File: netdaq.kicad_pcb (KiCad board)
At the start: 2 copper layers, 1 part, among them U1 PIC32CK1025GC01100-I/4SB

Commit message: did alot of stuff
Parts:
- added C1: 100n, Capacitor_SMD:C_0402_1005Metric, F.Cu at (186.1, 102.2)
- added C10: 100n, Capacitor_SMD:C_0402_1005Metric, F.Cu at (189.0, 108.1)
- added C11: 100n, Capacitor_SMD:C_0402_1005Metric, F.Cu at (189.0, 110.0)
- added C12: 100n, Capacitor_SMD:C_0402_1005Metric, F.Cu at (191.9, 102.2)
- added C13: 47u, Capacitor_SMD:C_1210_3225Metric, F.Cu at (181.9, 107.5)
- added C14: 100n, Capacitor_SMD:C_0402_1005Metric, F.Cu at (191.9, 104.1)
- added C15: 4.7u, Capacitor_SMD:C_0805_2012Metric, F.Cu at (186.9, 112.5)
- added C16: 100n, Capacitor_SMD:C_0402_1005Metric, F.Cu at (191.9, 106.1)
- added C17: 10u, Capacitor_SMD:C_0805_2012Metric, F.Cu at (186.9, 115.5)
- added C18: 47u, Capacitor_SMD:C_1210_3225Metric, F.Cu at (181.9, 111.8)
- added C19: C, Capacitor_SMD:C_0402_1005Metric, F.Cu at (180.2, 77.5)
- added C2: 100n, Capacitor_SMD:C_0402_1005Metric, F.Cu at (186.1, 104.1)
- added C20: C, Capacitor_SMD:C_0402_1005Metric, F.Cu at (180.2, 79.5)
- added C21: C, Capacitor_SMD:C_0402_1005Metric, F.Cu at (180.2, 81.4)
- added C22: C, Capacitor_SMD:C_0402_1005Metric, F.Cu at (180.2, 83.4)
- added C23: 1u, Capacitor_SMD:C_0603_1608Metric, F.Cu at (159.4, 72.5)
- added C24: C, Capacitor_SMD:C_0402_1005Metric, F.Cu at (172.4, 71.4)
- added C25: C, Capacitor_SMD:C_0402_1005Metric, F.Cu at (172.4, 73.4)
- added C26: 100n, Capacitor_SMD:C_0402_1005Metric, F.Cu at (172.4, 75.3)
- added C27: 100n, Capacitor_SMD:C_0402_1005Metric, F.Cu at (172.4, 77.3)
- added C28: 1u, Capacitor_SMD:C_0603_1608Metric, F.Cu at (159.4, 76.8)
- added C29: 1u, Capacitor_SMD:C_0603_1608Metric, F.Cu at (159.4, 81.0)
- added C3: 100n, Capacitor_SMD:C_0402_1005Metric, F.Cu at (186.1, 106.1)
- added C30: 100n, Capacitor_SMD:C_0402_1005Metric, F.Cu at (172.4, 79.3)
- added C31: 1u, Capacitor_SMD:C_0603_1608Metric, F.Cu at (159.4, 85.3)
- added C32: 470p, Capacitor_SMD:C_0402_1005Metric, F.Cu at (172.4, 81.3)
- added C4: 100n, Capacitor_SMD:C_0402_1005Metric, F.Cu at (186.1, 108.1)
- added C5: 100n, Capacitor_SMD:C_0402_1005Metric, F.Cu at (186.1, 110.0)
- added C6: 100n, Capacitor_SMD:C_0402_1005Metric, F.Cu at (189.0, 102.2)
- added C7: 100n, Capacitor_SMD:C_0402_1005Metric, F.Cu at (189.0, 104.1)
- added C8: 100n, Capacitor_SMD:C_0402_1005Metric, F.Cu at (189.0, 106.1)
- added C9: 47u, Capacitor_SMD:C_1210_3225Metric, F.Cu at (181.9, 103.3)
- added D1: LED, LED_SMD:LED_0805_2012Metric, F.Cu at (181.0, 71.9)
- added D2: LED, LED_SMD:LED_0805_2012Metric, F.Cu at (181.0, 75.0)
- added D3: LED, LED_SMD:LED_0805_2012Metric, F.Cu at (170.8, 85.9)
- added D4: LED, LED_SMD:LED_0805_2012Metric, F.Cu at (170.8, 88.9)
- added R1: 0, Resistor_SMD:R_0402_1005Metric, F.Cu at (190.6, 112.0)
- added R10: 1.5k, Resistor_SMD:R_0402_1005Metric, F.Cu at (163.7, 71.4)
- added R11: 1.5k, Resistor_SMD:R_0402_1005Metric, F.Cu at (163.7, 73.4)
- added R12: 33, Resistor_SMD:R_0402_1005Metric, F.Cu at (163.7, 75.4)
- added R13: 33, Resistor_SMD:R_0402_1005Metric, F.Cu at (163.7, 77.4)
- added R14: 33, Resistor_SMD:R_0402_1005Metric, F.Cu at (163.7, 79.4)
- added R15: 10k, Resistor_SMD:R_0402_1005Metric, F.Cu at (163.7, 81.4)
- added R16: 10k, Resistor_SMD:R_0402_1005Metric, F.Cu at (163.7, 83.4)
- added R17: 10k, Resistor_SMD:R_0402_1005Metric, F.Cu at (166.6, 71.4)
- added R18: 10k, Resistor_SMD:R_0402_1005Metric, F.Cu at (166.6, 73.4)
- added R19: 10k, Resistor_SMD:R_0402_1005Metric, F.Cu at (166.6, 75.4)
- added R2: 0, Resistor_SMD:R_0402_1005Metric, F.Cu at (190.6, 114.0)
- added R20: 10k, Resistor_SMD:R_0402_1005Metric, F.Cu at (166.6, 77.4)
- added R21: 1.5k, Resistor_SMD:R_0402_1005Metric, F.Cu at (166.6, 79.4)
- added R22: 10k, Resistor_SMD:R_0402_1005Metric, F.Cu at (166.6, 81.4)
- added R23: 10k, Resistor_SMD:R_0402_1005Metric, F.Cu at (166.6, 83.4)
- added R24: 12.1k, Resistor_SMD:R_0402_1005Metric, F.Cu at (169.6, 71.4)
- added R25: R, Resistor_SMD:R_0402_1005Metric, F.Cu at (169.6, 73.4)
- added R26: R, Resistor_SMD:R_0402_1005Metric, F.Cu at (169.6, 75.4)
- added R27: 10k, Resistor_SMD:R_0402_1005Metric, F.Cu at (169.6, 77.4)
- added R28: 10k, Resistor_SMD:R_0402_1005Metric, F.Cu at (169.6, 79.4)
- added R3: R, Resistor_SMD:R_0402_1005Metric, F.Cu at (177.3, 71.4)
- added R4: R, Resistor_SMD:R_0402_1005Metric, F.Cu at (177.3, 73.4)
- added R5: 10k, Resistor_SMD:R_0402_1005Metric, F.Cu at (177.3, 75.4)
- added R6: 10k, Resistor_SMD:R_0402_1005Metric, F.Cu at (177.3, 77.4)
- added R7: 270, Resistor_SMD:R_0402_1005Metric, F.Cu at (177.3, 79.4)
- added R8: 10k, Resistor_SMD:R_0402_1005Metric, F.Cu at (177.3, 81.4)
- added R9: 10k, Resistor_SMD:R_0402_1005Metric, F.Cu at (177.3, 83.4)
- added TR1: PT61017PEL, Transformer_SMD:Transformer_Ethernet_Bourns_PT61017PEL, F.Cu at (149.5, 79.5)
- added U2: LAN8720A-CP, LAN8720A-CP:QFN24-6X6_MC_MCH, F.Cu at (150.4, 91.5)
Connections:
- U1 pad 1: unconnected-(U1A-PA00-Pad1) -> /MCU/JTAG.TDI
- U1 pad 10: unconnected-(U1A-PA15-Pad10) -> /MCU/SPI5.SCK
- U1 pad 100: unconnected-(U1A-PD11-Pad100) -> /MCU/SDMMC0_SDDAT1
- U1 pad 11: unconnected-(U1A-PA16-Pad11) -> /MCU/SPI5.CS#
- U1 pad 12: unconnected-(U1A-PA17-Pad12) -> /MCU/SPARE1
- U1 pad 13: unconnected-(U1A-PA04-Pad13) -> /MCU/SPI7.MISO
- U1 pad 14: unconnected-(U1A-PA05-Pad14) -> /MCU/SPI7.SCK
- U1 pad 15: unconnected-(U1A-PA06-Pad15) -> /MCU/SPI7.CS#
- U1 pad 16: unconnected-(U1A-PA07-Pad16) -> /MCU/SPI6.MOSI
- U1 pad 17: unconnected-(U1A-PA08-Pad17) -> /MCU/SPI6.MISO
- U1 pad 18: unconnected-(U1A-PA18-Pad18) -> /MCU/SPARE2
- U1 pad 2: unconnected-(U1A-PA01-Pad2) -> /MCU/PA01
- U1 pad 20: unconnected-(U1B-VDDIO-Pad20) -> +3.3V
- U1 pad 21: unconnected-(U1A-EXT-Pad21) -> /MCU/EXT
- U1 pad 22: unconnected-(U1A-PA09-Pad22) -> /MCU/SPI6.SCK
- U1 pad 23: unconnected-(U1A-PA10-Pad23) -> /MCU/SPI6.CS#
- U1 pad 24: unconnected-(U1A-PA11-Pad24) -> /SMI.MDC
- U1 pad 25: unconnected-(U1A-PA12-Pad25) -> /SMI.MDIO
- U1 pad 26: unconnected-(U1A-PB00-Pad26) -> /MCU/SPARE12
- U1 pad 27: unconnected-(U1A-PB01-Pad27) -> /MCU/SPARE13
- U1 pad 28: unconnected-(U1A-PB11-Pad28) -> /MCU/ADC_VINP10
- U1 pad 29: unconnected-(U1A-PB12-Pad29) -> /MCU/ADC_VINP11
- U1 pad 3: unconnected-(U1A-PA02-Pad3) -> /MCU/JTAG.TMS
- U1 pad 31: unconnected-(U1A-PB02-Pad31) -> /MCU/XIN32
- U1 pad 32: unconnected-(U1A-PB03-Pad32) -> /MCU/XOUT32
- U1 pad 33: unconnected-(U1B-VDDA-Pad33) -> Net-(U1B-VDDA)
- U1 pad 34: unconnected-(U1B-VDDIO-Pad34) -> +3.3V
- U1 pad 36: unconnected-(U1A-PB04-Pad36) -> /MCU/SPI4.MOSI
- U1 pad 37: unconnected-(U1A-PB05-Pad37) -> /MCU/SPI4.MISO
- U1 pad 38: unconnected-(U1A-PB13-Pad38) -> /MCU/SPI4.SCK
- U1 pad 39: unconnected-(U1A-PB06-Pad39) -> /MCU/SPI4.CS#
- U1 pad 4: unconnected-(U1A-PA03-Pad4) -> /MCU/JTAG.TCK
- U1 pad 40: unconnected-(U1A-PB14-Pad40) -> /MCU/SPARE16
- U1 pad 41: unconnected-(U1A-PB15-Pad41) -> /MCU/SPARE17
- U1 pad 42: unconnected-(U1B-VDDIO-Pad42) -> +3.3V
- U1 pad 44: unconnected-(U1B-VDDREG-Pad44) -> +3.3V
- U1 pad 45: unconnected-(U1A-PB16-Pad45) -> /MCU/SPI3.MOSI
- U1 pad 46: unconnected-(U1A-PB17-Pad46) -> /MCU/SPI3.MISO
- U1 pad 47: unconnected-(U1A-PB07-Pad47) -> /MCU/SPI3.SCK
- U1 pad 48: unconnected-(U1A-PB08-Pad48) -> /MCU/SPI3.CS#
- U1 pad 49: unconnected-(U1A-PB09-Pad49) -> /MCU/SPARE14
- U1 pad 5: unconnected-(U1A-RESET_N-Pad5) -> /MCU/RESET#
- U1 pad 50: unconnected-(U1A-PB10-Pad50) -> /MCU/SPARE15
- U1 pad 51: unconnected-(U1A-PC00-Pad51) -> /MCU/RMII.REFCK
- U1 pad 52: unconnected-(U1A-PC01-Pad52) -> /MCU/SPARE4
- U1 pad 53: unconnected-(U1A-PC02-Pad53) -> /MCU/SPARE5
- U1 pad 54: unconnected-(U1A-PC03-Pad54) -> /MCU/SPARE6
- U1 pad 55: unconnected-(U1A-PC04-Pad55) -> /MCU/SPARE7
- U1 pad 56: unconnected-(U1B-VDDIO-Pad56) -> +3.3V
- U1 pad 58: unconnected-(U1A-PC14-Pad58) -> /MCU/SPARE9
- U1 pad 59: unconnected-(U1A-PC05-Pad59) -> /MCU/SPARE8
- U1 pad 60: unconnected-(U1A-PC06-Pad60) -> /MCU/RMII.RXD1
- U1 pad 61: unconnected-(U1A-PC07-Pad61) -> /MCU/RMII.RXD0
- U1 pad 62: unconnected-(U1B-VDDREG-Pad62) -> +3.3V
- U1 pad 63: unconnected-(U1A-PC09-Pad63) -> /MCU/RMII.RXER
- U1 pad 64: unconnected-(U1A-PC15-Pad64) -> /MCU/SPI2.MOSI
- U1 pad 65: unconnected-(U1A-PC16-Pad65) -> /MCU/SPI2.MISO
- U1 pad 66: unconnected-(U1A-PC17-Pad66) -> /MCU/SPI2.SCK
- U1 pad 67: unconnected-(U1A-PC18-Pad67) -> /MCU/SPI2.CS#
- U1 pad 68: unconnected-(U1A-PC10-Pad68) -> /MCU/RMII.CRSDV
- U1 pad 69: unconnected-(U1B-VDDIO-Pad69) -> +3.3V
- U1 pad 7: unconnected-(U1B-VDDIO-Pad7) -> +3.3V
- U1 pad 71: unconnected-(U1A-PC11-Pad71) -> /MCU/RMII.TXEN
- U1 pad 72: unconnected-(U1A-PC12-Pad72) -> /MCU/RMII.TXD0
- U1 pad 73: unconnected-(U1A-PC13-Pad73) -> /MCU/RMII.TXD1
- U1 pad 74: unconnected-(U1A-PC19-Pad74) -> /MCU/SPARE10
- U1 pad 75: unconnected-(U1A-PC20-Pad75) -> /MCU/SPARE11
- U1 pad 76: unconnected-(U1A-USB0PN-Pad76) -> /MCU/USB_HS.D-
- U1 pad 77: unconnected-(U1A-USB0PP-Pad77) -> /MCU/USB_HS.D+
- U1 pad 78: unconnected-(U1A-USB0ID-Pad78) -> /MCU/USB0ID
- U1 pad 79: unconnected-(U1B-VCCAP3-Pad79) -> +3.3V
- U1 pad 8: unconnected-(U1A-PA13-Pad8) -> /MCU/SPI5.MOSI
- U1 pad 82: unconnected-(U1A-USRBIAS-Pad82) -> /MCU/USRBIAS
- U1 pad 83: unconnected-(U1B-VDDREG-Pad83) -> +3.3V
- U1 pad 85: unconnected-(U1B-VDDIO-Pad85) -> +3.3V
- U1 pad 86: unconnected-(U1A-PD00-Pad86) -> /MCU/XIN
- U1 pad 87: unconnected-(U1A-PD01-Pad87) -> /MCU/XOUT
- U1 pad 88: unconnected-(U1A-PD02-Pad88) -> /MCU/ETH_TSUCOMP
- U1 pad 89: unconnected-(U1A-USB_DM-Pad89) -> /MCU/USB_FS.D-
- U1 pad 9: unconnected-(U1A-PA14-Pad9) -> /MCU/SPI5.MISO
- U1 pad 90: unconnected-(U1A-USB_DP-Pad90) -> /MCU/USB_FS.D+
- U1 pad 91: unconnected-(U1A-PD12-Pad91) -> /MCU/SDMMC0_SDCD
- U1 pad 92: unconnected-(U1A-PD05-Pad92) -> /MCU/SDMMC0_SDWP
- U1 pad 93: unconnected-(U1A-PD06-Pad93) -> /MCU/SDMMC0_SDCMD
- U1 pad 94: unconnected-(U1A-PD07-Pad94) -> /MCU/SDMMC0_SDDAT0
- U1 pad 96: unconnected-(U1B-VDDIO-Pad96) -> +3.3V
- U1 pad 97: unconnected-(U1A-PD08-Pad97) -> /MCU/SDMMC0_SDDAT2
- U1 pad 98: unconnected-(U1A-PD09-Pad98) -> /MCU/SDMMC0_SDDAT3
- U1 pad 99: unconnected-(U1A-PD10-Pad99) -> /MCU/SDMMC0_SDCK

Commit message: did stuff
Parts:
- added J1: RJ45, Connector_RJ:RJ45_Amphenol_54602-x08_Horizontal, F.Cu at (153.3, 66.1)
- added J2: ~, pxc_1713856_02_01_DMC-1-5-19-G1F-3-5-LR-P26THR:pxc_1713856_02_01_DMC-1-5-19-G1F-3-5-LR-P26THR, F.Cu at (170.0, 140.0)
- added TR2: Wuerth_750343373, Transformer_THT:Transformer_Wuerth_750343373, F.Cu at (170.8, 63.8)
- added U3: MP6004GQ-P, MP6004GQ-P:QFN-14_MP6004_MNP, F.Cu at (169.4, 86.0)
- moved C19 59.3 mm to (238.5, 88.1)
- moved C20 59.3 mm to (238.5, 90.1)
- moved C23 59.3 mm to (217.8, 83.2)
- moved C24 59.3 mm to (230.7, 82.0)
- moved C25 59.3 mm to (230.7, 84.0)
- moved C26 59.3 mm to (230.7, 86.0)
- moved C27 59.3 mm to (230.7, 87.9)
- moved C28 59.3 mm to (217.8, 87.4)
- moved C29 59.3 mm to (217.8, 91.7)
- moved C31 59.3 mm to (217.8, 95.9)
- moved D1 59.3 mm to (239.3, 82.5)
- moved R11 59.3 mm to (222.0, 84.0)
- moved R14 59.3 mm to (222.0, 90.0)
- moved R18 59.3 mm to (224.9, 84.0)
- moved R21 59.3 mm to (224.9, 90.0)
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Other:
- board outline added: 72 x 83 mm

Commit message: did stuff
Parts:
- added U4: PD70100ILD-TR, PD70100ILD-TR:DFN12_4X3_MCH, F.Cu at (143.1, 102.2)
- added U5: ~, CDHD01:CDHD01, F.Cu at (138.8, 94.0)
- added U6: ~, CDHD01:CDHD01, F.Cu at (137.8, 79.5)
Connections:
- net Net-(D5-A) renamed /PoE Regulator/FLY_SW
- net Net-(R38-Pad1) renamed /PoE Regulator/FLY_CT
- net Net-(U3-FB1) renamed /PoE Regulator/FLY_FB
- net Net-(U3-VCC) renamed /PoE Regulator/FLY_VCC

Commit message: stuff
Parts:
- added U7: TPS62A01PDDCR, TPS62A01PDDCR:DDC0006A-MFG, F.Cu at (142.8, 116.0)
- moved C19 77.4 mm to (170.8, 125.4)
- moved C20 77.4 mm to (170.8, 127.4)
- moved C21 77.4 mm to (170.8, 129.4)
- moved C22 77.4 mm to (170.8, 131.3)
- moved C23 77.4 mm to (150.0, 120.5)
- moved C24 77.4 mm to (163.0, 119.4)
- moved C25 77.4 mm to (163.0, 121.3)
- moved C26 77.4 mm to (163.0, 123.3)
- moved C27 77.4 mm to (163.0, 125.3)
- moved C28 77.4 mm to (150.0, 124.8)
- moved C29 77.4 mm to (150.0, 129.0)
- moved C30 77.4 mm to (163.0, 127.2)
- moved C31 77.4 mm to (150.0, 133.2)
- moved C32 77.4 mm to (163.0, 129.2)
- moved D1 77.4 mm to (171.6, 119.9)
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
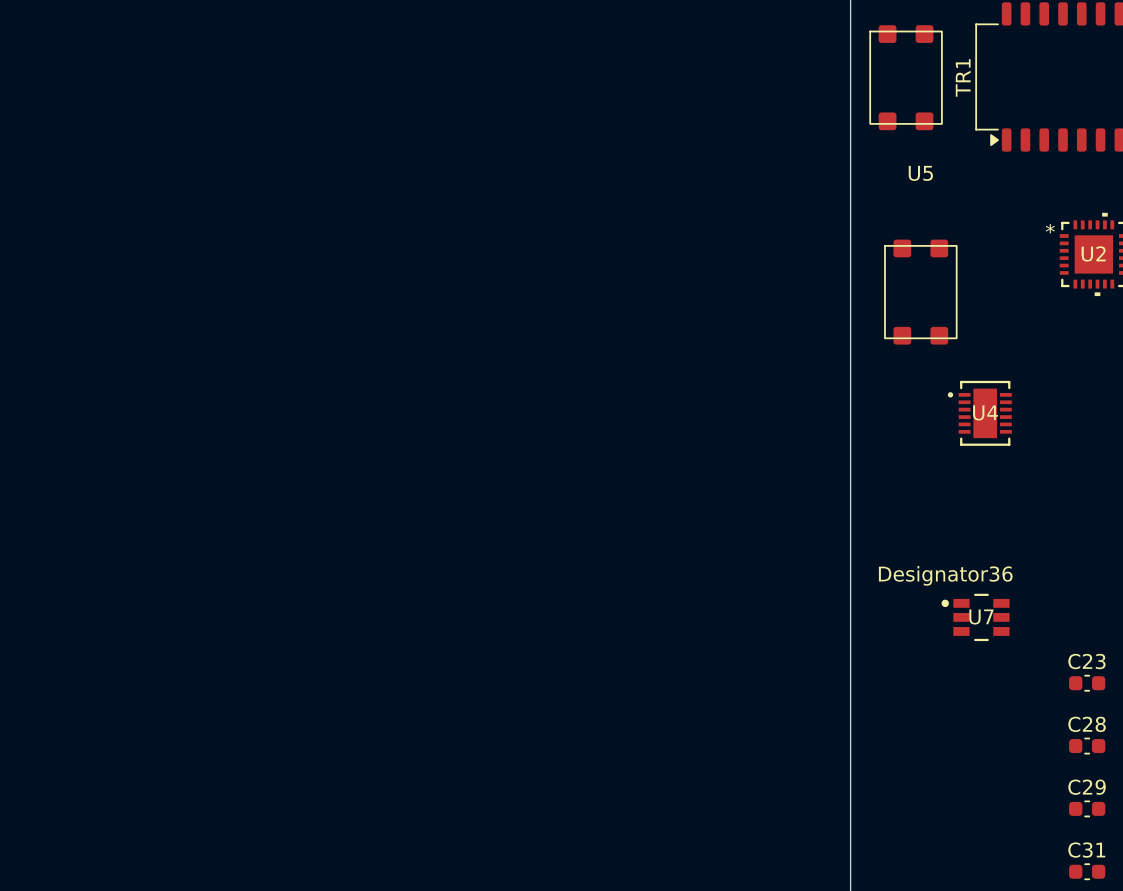
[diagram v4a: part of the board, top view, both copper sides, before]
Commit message: did 3v3 reg
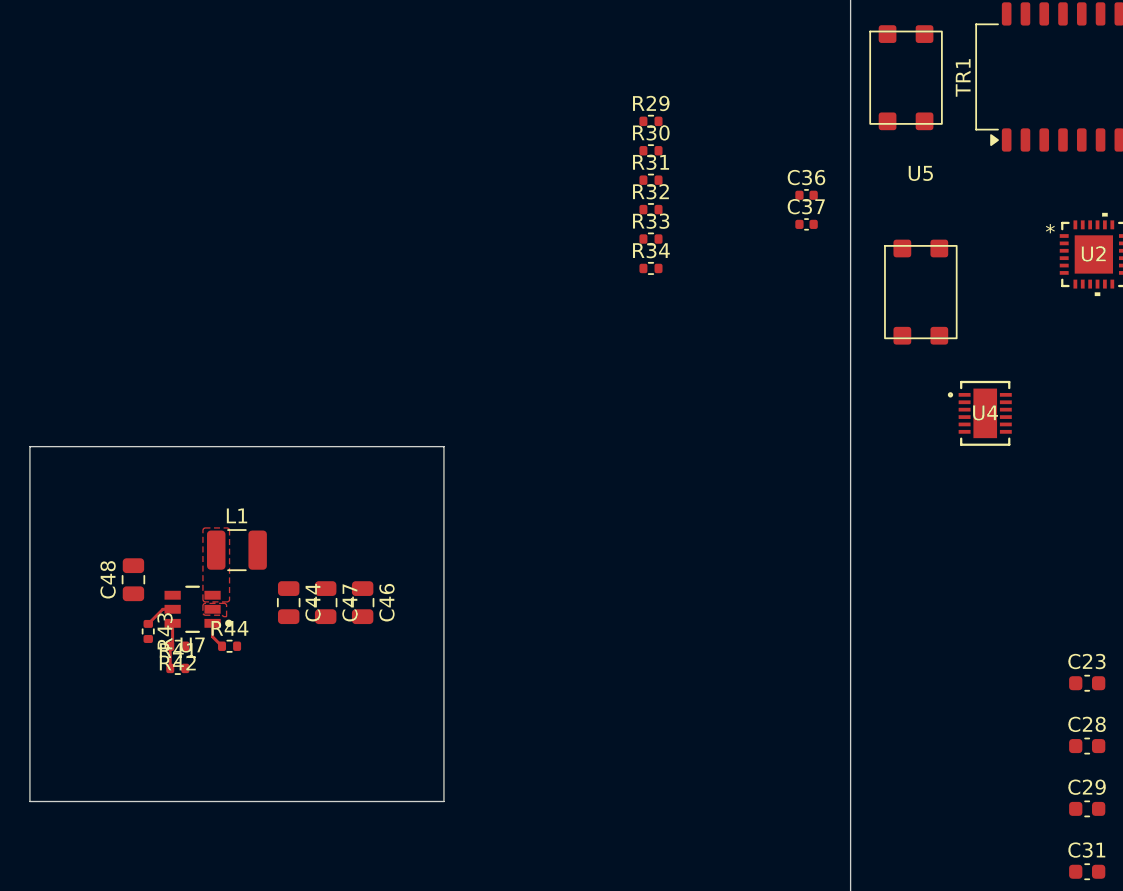
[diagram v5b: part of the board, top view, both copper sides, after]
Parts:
- added C36: 100n, Capacitor_SMD:C_0402_1005Metric, F.Cu at (131.0, 87.5)
- added C37: 100n, Capacitor_SMD:C_0402_1005Metric, F.Cu at (131.0, 89.5)
- added C44: 10u, Capacitor_SMD:C_0805_2012Metric, F.Cu at (96.0, 115.0)
- added C46: 10u, Capacitor_SMD:C_0805_2012Metric, F.Cu at (101.0, 115.0)
- added C47: 10u, Capacitor_SMD:C_0805_2012Metric, F.Cu at (98.5, 115.0)
- added C48: 10u, Capacitor_SMD:C_0805_2012Metric, F.Cu at (85.5, 113.5)
- added L1: 1u, Inductor_SMD:L_1210_3225Metric, F.Cu at (92.5, 111.5)
- added R29: 75, Resistor_SMD:R_0402_1005Metric, F.Cu at (120.5, 82.5)
- added R30: 75, Resistor_SMD:R_0402_1005Metric, F.Cu at (120.5, 84.5)
- added R31: 75, Resistor_SMD:R_0402_1005Metric, F.Cu at (120.5, 86.5)
- added R32: 75, Resistor_SMD:R_0402_1005Metric, F.Cu at (120.5, 88.5)
- added R33: 0, Resistor_SMD:R_0402_1005Metric, F.Cu at (120.5, 90.5)
- added R34: 0, Resistor_SMD:R_0402_1005Metric, F.Cu at (120.5, 92.5)
- added R41: 453k, Resistor_SMD:R_0402_1005Metric, F.Cu at (88.5, 119.5)
- added R42: 100k, Resistor_SMD:R_0402_1005Metric, F.Cu at (88.5, 118.0)
- added R43: 100k, Resistor_SMD:R_0402_1005Metric, F.Cu at (86.5, 117.0)
- added R44: 100k, Resistor_SMD:R_0402_1005Metric, F.Cu at (92.0, 118.0)
- moved U7 53.4 mm to (89.5, 115.5), turned to 180 degrees
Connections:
- U7 pad 1: unconnected-(U7-EN-Pad1) -> /3V3 Regulator/3V3_EN
- U7 pad 2: unconnected-(U7-GND-Pad2) -> GND
- U7 pad 3: unconnected-(U7-SW-Pad3) -> /3V3 Regulator/3V3_SW
- U7 pad 4: unconnected-(U7-VIN-Pad4) -> +5.0V
- U7 pad 5: unconnected-(U7-PG-Pad5) -> /3V3 Regulator/3V3_PG
- U7 pad 6: unconnected-(U7-FB-Pad6) -> /3V3 Regulator/3V3_FB
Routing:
- net /3V3 Regulator/3V3_FB: track 0.00 -> 3.12 mm
- net /3V3 Regulator/3V3_PG: track 0.00 -> 2.06 mm
- net /3V3 Regulator/3V3_EN: track 0.00 -> 1.82 mm
- added copper zone on F.Cu, net /3V3 Regulator/3V3_SW
- added copper zone on F.Cu, net GND
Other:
- board size 72 x 83 mm -> 127.5 x 83 mm
- board text added: "3v3"

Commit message: stuff
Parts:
- added C49: 100n, Capacitor_SMD:C_0402_1005Metric, F.Cu at (231.5, 118.0)
- added C50: 10u, Capacitor_SMD:C_0805_2012Metric, F.Cu at (232.3, 115.5)
- added J3: Conn_01x06_Pin, Connector_PinHeader_2.54mm:PinHeader_1x06_P2.54mm_Vertical, F.Cu at (42.0, 120.3)
- added J4: Micro_SD_Card_Det2, Connector_Card:microSD_HC_Hirose_DM3AT-SF-PEJM5, F.Cu at (221.7, 107.4)
- added R1: 0, Resistor_SMD:R_0402_1005Metric, F.Cu at (129.5, 69.0)
- added R45: 100k, Resistor_SMD:R_0402_1005Metric, F.Cu at (231.5, 99.1)
- added R46: 10k, Resistor_SMD:R_0402_1005Metric, F.Cu at (231.5, 101.1)
- added R47: 10k, Resistor_SMD:R_0402_1005Metric, F.Cu at (231.5, 103.1)
- added R48: 10k, Resistor_SMD:R_0402_1005Metric, F.Cu at (231.5, 105.0)
- added R49: 10k, Resistor_SMD:R_0402_1005Metric, F.Cu at (231.5, 107.0)
- added R50: 10k, Resistor_SMD:R_0402_1005Metric, F.Cu at (231.5, 109.0)
- added R51: 10k, Resistor_SMD:R_0402_1005Metric, F.Cu at (231.5, 111.0)
- added R52: 10k, Resistor_SMD:R_0402_1005Metric, F.Cu at (231.5, 113.0)
- added R53: 0, Resistor_SMD:R_0402_1005Metric, F.Cu at (129.5, 71.0)
- added R54: 0, Resistor_SMD:R_0402_1005Metric, F.Cu at (129.5, 73.0)
- added R55: 0, Resistor_SMD:R_0402_1005Metric, F.Cu at (129.5, 75.0)
- added R56: 27, Resistor_SMD:R_0402_1005Metric, F.Cu at (56.5, 54.0)
- added R57: 27, Resistor_SMD:R_0402_1005Metric, F.Cu at (55.0, 55.5)
- added R58: 27, Resistor_SMD:R_0402_1005Metric, F.Cu at (57.0, 54.5)
- added R59: 27, Resistor_SMD:R_0402_1005Metric, F.Cu at (55.5, 56.0)
- moved C12 125.9 mm to (72.5, 62.1)
- moved C13 125.9 mm to (62.5, 67.4)
- moved C14 125.9 mm to (72.5, 64.0)
- moved C18 125.9 mm to (62.5, 71.7)
- moved C9 125.9 mm to (62.5, 63.2)
- moved C1 125.9 mm to (66.8, 62.1)
- moved C16 125.9 mm to (72.5, 66.0)
- moved C19 125.9 mm to (51.4, 85.3)
- moved C2 125.9 mm to (66.8, 64.0)
- moved C20 125.9 mm to (51.4, 87.3)
- moved C21 125.9 mm to (51.4, 89.3)
- moved C22 125.9 mm to (51.4, 91.3)
- moved C6 125.9 mm to (69.7, 62.1)
- moved C7 125.9 mm to (69.7, 64.0)
- moved D1 125.9 mm to (52.3, 79.8)
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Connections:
- net /MCU/SDMMC0_SDWP renamed /SDMMC.SDWP
- net /MCU/SPI4.CS# renamed /MCU/NC_SERCOM4_PAD3
- net /MCU/SPI4.MISO renamed /MCU/UART4.RX
- net /MCU/SPI4.MOSI renamed /MCU/UART4.TX
- net /MCU/SPI4.SCK renamed /MCU/NC_SERCOM4_PAD2
- net /MCU/SPI7.CS# renamed /MCU/NC_SERCOM7_PAD3
- net /MCU/SPI7.MISO renamed /MCU/I2C7.SDA
- net /MCU/SPI7.SCK renamed /MCU/I2C7.SCL
- net Net-(TR1-C_RX) renamed /Ethernet Connector/CTREF1
- net Net-(TR1-C_TX) renamed /Ethernet Connector/CTREF2
- U1 pad 100: /MCU/SDMMC0_SDDAT1 -> /SDMMC.SDDAT1
- U1 pad 91: /MCU/SDMMC0_SDCD -> /SDMMC.SDCD
- U1 pad 93: /MCU/SDMMC0_SDCMD -> /SDMMC.SDCMD
- U1 pad 94: /MCU/SDMMC0_SDDAT0 -> /SDMMC.SDDAT0
- U1 pad 97: /MCU/SDMMC0_SDDAT2 -> /SDMMC.SDDAT2
- U1 pad 98: /MCU/SDMMC0_SDDAT3 -> /SDMMC.SDDAT3
- U1 pad 99: /MCU/SDMMC0_SDCK -> /SDMMC.SDCK
- U5 pad 1: unconnected-(U5-+-Pad1) -> /Ethernet Connector/POE_V+
- U5 pad 2: unconnected-(U5---Pad2) -> /Ethernet Connector/POE_V-
- U5 pad 3: unconnected-(U5-Pad3) -> Net-(R55-Pad1)
- U5 pad 4: unconnected-(U5-Pad4) -> Net-(R54-Pad1)
- U6 pad 1: unconnected-(U6-+-Pad1) -> /Ethernet Connector/POE_V+
- U6 pad 2: unconnected-(U6---Pad2) -> /Ethernet Connector/POE_V-
- U6 pad 3: unconnected-(U6-Pad3) -> /Ethernet Connector/POE_CT2
- U6 pad 4: unconnected-(U6-Pad4) -> /Ethernet Connector/POE_CT1
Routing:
- net /MCU/USB_FS.D-: track 0.00 -> 0.01 mm, vias 0 -> 1
- net /MCU/USB_FS.D+: track 0.00 -> 0.01 mm, vias 0 -> 1

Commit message: pcb constraints
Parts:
- moved C19 34.5 mm to (84.0, 74.0)
- moved C20 34.5 mm to (84.0, 76.0)
- moved C21 34.5 mm to (84.0, 78.0)
- moved C22 34.5 mm to (84.0, 79.9)
- moved D1 34.5 mm to (84.8, 68.5)
- moved D2 34.5 mm to (84.8, 71.5)
- moved R3 34.5 mm to (81.1, 68.0)
- moved R4 34.5 mm to (81.1, 70.0)
- moved R5 34.5 mm to (81.1, 71.9)
- moved R6 34.5 mm to (81.1, 73.9)
- moved R7 34.5 mm to (81.1, 75.9)
- moved R8 34.5 mm to (81.1, 77.9)
- moved R9 34.5 mm to (81.1, 79.9)
- moved C9 21.0 mm to (80.5, 52.2)
- moved C13 21.0 mm to (80.5, 56.5)
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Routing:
- net +3.3V: track 0.00 -> 4.44 mm, vias 0 -> 45
- net +5.0V: track 0.00 -> 0.91 mm, vias 0 -> 1
- added copper zone on F.Cu, net +3.3V
- added copper zone on F.Cu, net +5.0V

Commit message: started on adc
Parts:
- added C51: 1u, Capacitor_SMD:C_0603_1608Metric, F.Cu at (102.5, 176.5)
- added C52: 1u, Capacitor_SMD:C_0603_1608Metric, F.Cu at (98.5, 180.5)
- added C53: 1u, Capacitor_SMD:C_0603_1608Metric, F.Cu at (101.0, 180.5)
- added C54: 1u, Capacitor_SMD:C_0603_1608Metric, F.Cu at (92.5, 176.5)
- added C55: 1u, Capacitor_SMD:C_0603_1608Metric, F.Cu at (88.5, 180.5)
- added C56: 1u, Capacitor_SMD:C_0603_1608Metric, F.Cu at (91.0, 180.5)
- added C57: 1u, Capacitor_SMD:C_0603_1608Metric, F.Cu at (102.5, 196.0)
- added C58: 1u, Capacitor_SMD:C_0603_1608Metric, F.Cu at (98.5, 200.0)
- added C59: 1u, Capacitor_SMD:C_0603_1608Metric, F.Cu at (101.0, 200.0)
- added C60: 1u, Capacitor_SMD:C_0603_1608Metric, F.Cu at (102.5, 186.6)
- added C61: 1u, Capacitor_SMD:C_0603_1608Metric, F.Cu at (98.5, 190.5)
- added C62: 1u, Capacitor_SMD:C_0603_1608Metric, F.Cu at (101.0, 190.5)
- added U10: TLA2518IRTER, TLA2518IRTER:WQFN16_RTE_TEX, F.Cu at (98.0, 195.5)
- added U11: TLA2518IRTER, TLA2518IRTER:WQFN16_RTE_TEX, F.Cu at (98.0, 186.0)
- added U8: TLA2518IRTER, TLA2518IRTER:WQFN16_RTE_TEX, F.Cu at (98.0, 176.0)
- added U9: TLA2518IRTER, TLA2518IRTER:WQFN16_RTE_TEX, F.Cu at (88.0, 176.0)
- moved R1 229.1 mm to (358.0, 85.5)
- moved R29 229.1 mm to (349.0, 99.0)
- moved R30 229.1 mm to (349.0, 101.0)
- moved R31 229.1 mm to (349.0, 103.0)
- moved R32 229.1 mm to (349.0, 105.0)
- moved R33 229.1 mm to (349.0, 107.0)
- moved R34 229.1 mm to (349.0, 109.0)
- moved R53 229.1 mm to (358.0, 87.5)
- moved R54 229.1 mm to (358.0, 89.5)
- moved R55 229.1 mm to (358.0, 91.5)
- moved C36 229.1 mm to (359.5, 104.0)
- moved C37 229.1 mm to (359.5, 106.0)
- moved U5 206.8 mm to (345.5, 91.5)
- moved U6 206.8 mm to (344.5, 77.0)
- moved TR2 205.5 mm to (325.3, 199.2)
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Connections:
- U1 pad 10: /MCU/SPI5.SCK -> /ADC3/SPI.SCK
- U1 pad 11: /MCU/SPI5.CS# -> /ADC3/SPI.CS#
- U1 pad 16: /MCU/SPI6.MOSI -> /ADC4/SPI.MOSI
- U1 pad 17: /MCU/SPI6.MISO -> /ADC4/SPI.MISO
- U1 pad 22: /MCU/SPI6.SCK -> /ADC4/SPI.SCK
- U1 pad 23: /MCU/SPI6.CS# -> /ADC4/SPI.CS#
- U1 pad 45: /MCU/SPI3.MOSI -> /ADC2/SPI.MOSI
- U1 pad 46: /MCU/SPI3.MISO -> /ADC2/SPI.MISO
- U1 pad 47: /MCU/SPI3.SCK -> /ADC2/SPI.SCK
- U1 pad 48: /MCU/SPI3.CS# -> /ADC2/SPI.CS#
- U1 pad 64: /MCU/SPI2.MOSI -> /ADC1/SPI.MOSI
- U1 pad 65: /MCU/SPI2.MISO -> /ADC1/SPI.MISO
- U1 pad 66: /MCU/SPI2.SCK -> /ADC1/SPI.SCK
- U1 pad 67: /MCU/SPI2.CS# -> /ADC1/SPI.CS#
- U1 pad 8: /MCU/SPI5.MOSI -> /ADC3/SPI.MOSI
- U1 pad 9: /MCU/SPI5.MISO -> /ADC3/SPI.MISO
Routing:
- net +3.3V: track 4.44 -> 37.8 mm
- net Net-(U1B-VDDA): track 0.00 -> 2.42 mm
